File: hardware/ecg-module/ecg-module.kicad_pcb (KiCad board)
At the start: 2 copper layers, 58 x 58 mm, 45 parts, among them IC1 AP2112K-1.8TRG1, J1 ST_01x02, J2 LEFT-UI, J3 RIGHT-UI

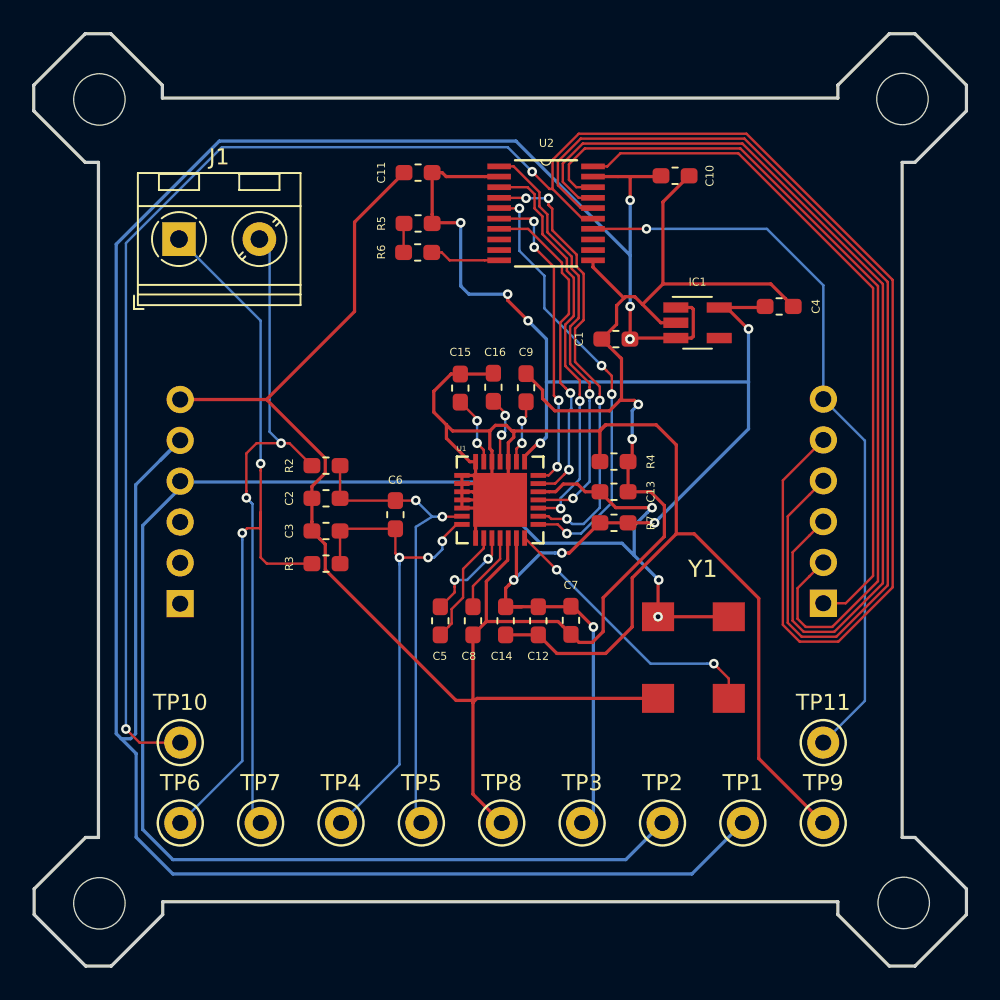
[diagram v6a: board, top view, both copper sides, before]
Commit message: Add copper pour of bottom layer
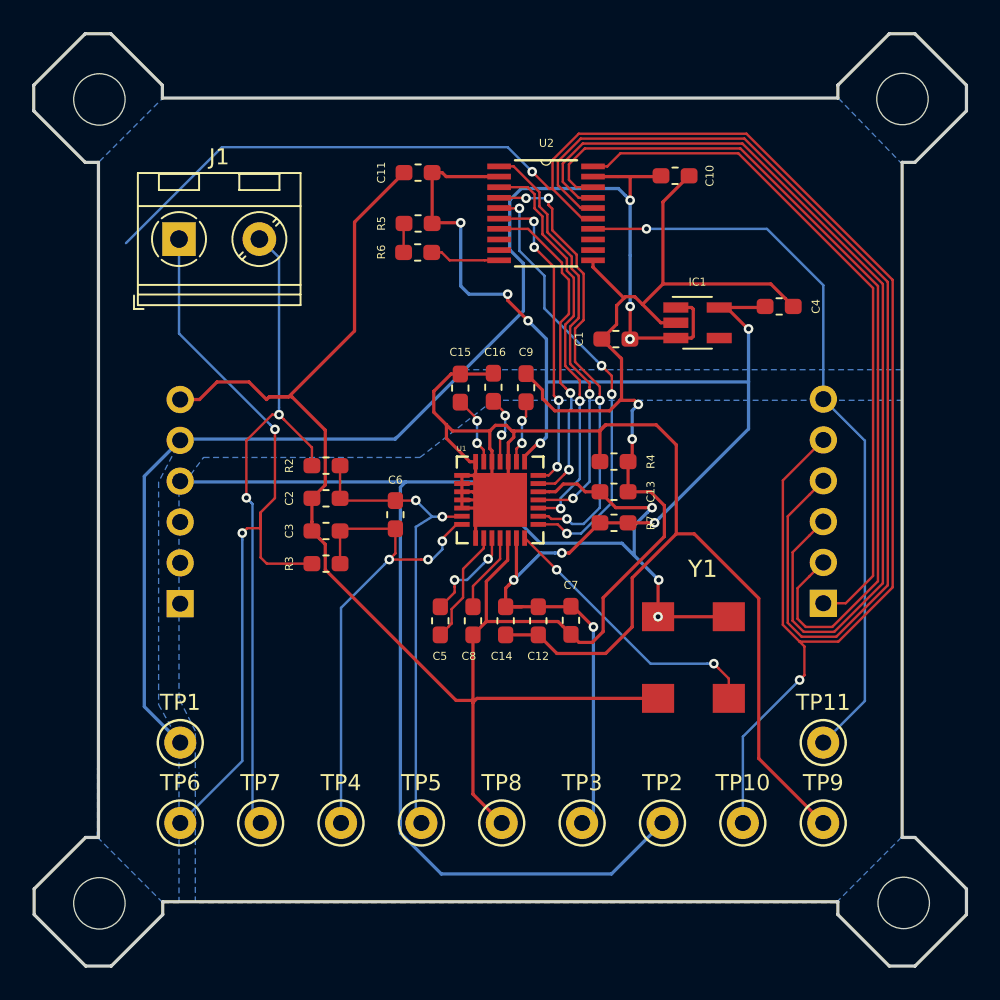
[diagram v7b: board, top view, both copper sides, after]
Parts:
- moved TP1 35.4 mm to (128.6, 120.1)
- moved TP10 35.4 mm to (163.6, 125.1)
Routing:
- net +5V: track 158.5 -> 82.0 mm
- net INTB_5V: track 135.1 -> 114.1 mm
- net +3V3: track 106.8 -> 91.2 mm
- net GND: track 146.3 -> 148.8 mm
- net Net-(J1-Pad2): track 41.5 -> 42.3 mm
- net Net-(J1-Pad1): track 47.2 -> 47.9 mm
- added copper zone on B.Cu, net +3V3
- added copper zone on B.Cu, net +5V

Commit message: Add copper pour of top layer
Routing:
- net +3V3: track 91.2 -> 93.3 mm
- net Net-(C3-Pad1): track 31.1 -> 29.5 mm, vias 3 -> 1
- net GND: track 148.8 -> 150.3 mm
- net +1V8: track 94.7 -> 93.3 mm, vias 9 -> 7
- net Net-(J1-Pad1): track 47.9 -> 46.5 mm
- net GNDA: track 102.6 -> 103.6 mm
- net MOSI_1.8V: track 25.5 -> 26.2 mm
- net MISO_1.8V: track 26.6 -> 27.2 mm
- net Net-(C2-Pad2): track 29.1 -> 29.4 mm, vias 2 -> 1
